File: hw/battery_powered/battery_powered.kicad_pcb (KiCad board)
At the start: 2 copper layers, 56 x 71.5 mm, 64 parts, among them J101 5077CR-16SMC2-BK-TR, J102 battery_wire_pad, J103 BM03B-SRSS-TB(LF)(SN)_pico_de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, J104 10029449-111RLF, SW101 SS12D01G4, SW102 SKRPABE010, SW103 SKRPABE010, SW104 SKRPABE010, U101 RT6150B-33GQW, U102 W25Q16JVSNIQ, U103 RP2040, U104 PCA9306D, U105 OSL10564-IB, U106 chofutech_logo, Y101 FA-238V

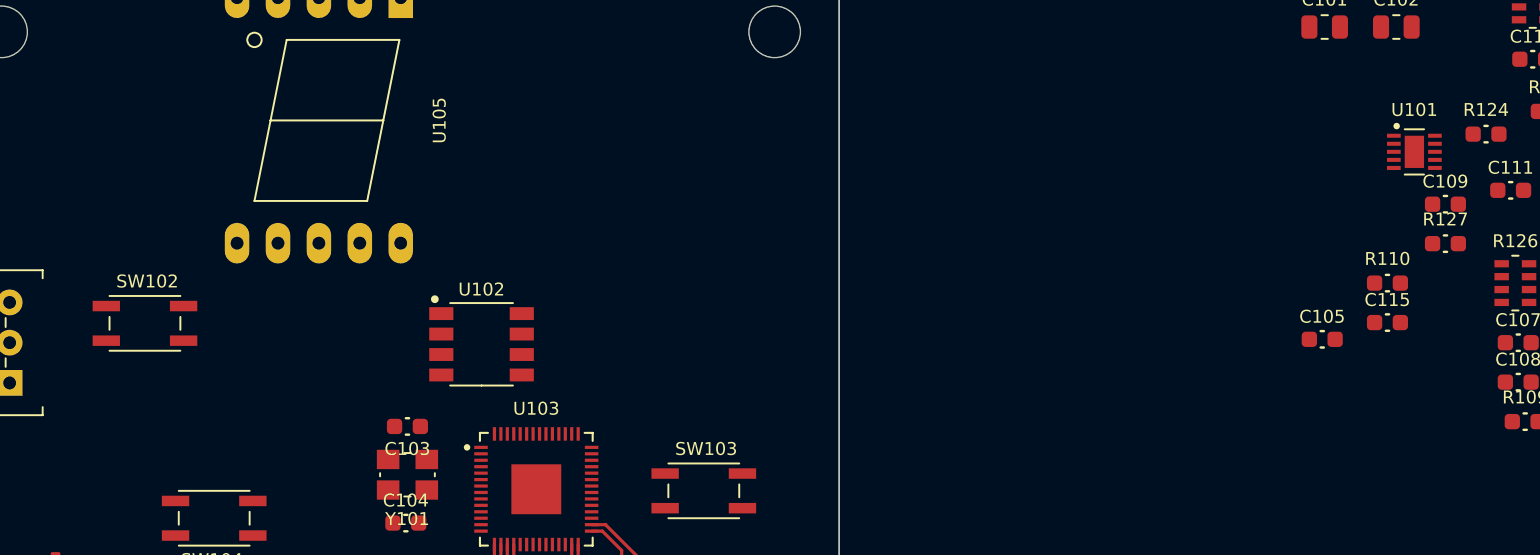
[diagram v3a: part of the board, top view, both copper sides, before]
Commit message: fixed battery_powered artwork and add .gitkeep to build dir
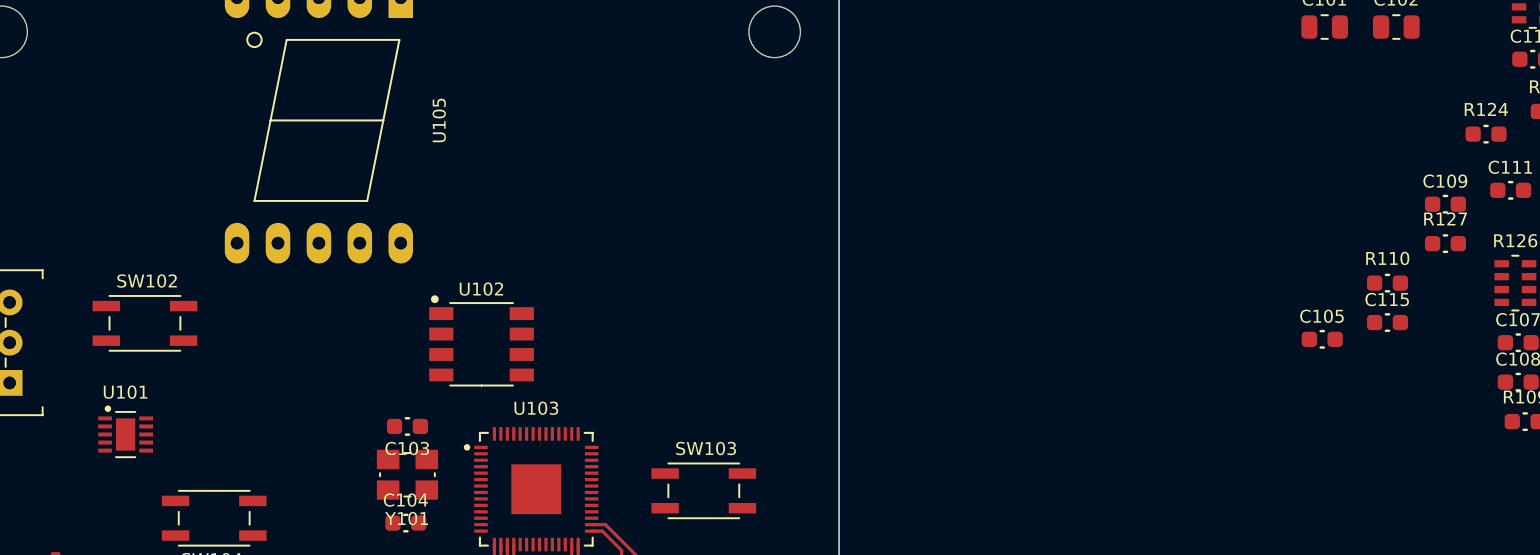
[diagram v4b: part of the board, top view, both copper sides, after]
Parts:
- moved U101 81.9 mm to (61.7, 89.0)
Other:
- copper layers 2 -> 4
- board text added: "Assumes jlcpcb 4-layer impedance control setup JLC7628. surface copper : 0.035 mm inner copper : 0.0152 mm prepreg : 0.2mm Er:4.6 core : 0.7mm Er:4.6"
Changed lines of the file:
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@@
 (kicad_pcb (version 20211014) (generator pcbnew)
   (general
-    (thickness 1.6)
+    (thickness 3.0152)
   )
   (paper "A4")
   (layers
     (0 "F.Cu" signal)
+    (1 "In1.Cu" signal)
+    (2 "In2.Cu" signal)
     (31 "B.Cu" signal)
     (32 "B.Adhes" user "B.Adhesive")
@@
       (layer "F.SilkS" (type "Top Silk Screen"))
       (layer "F.Paste" (type "Top Solder Paste"))
-      (layer "F.Mask" (type "Top Solder Mask") (thickness 0.01))
+      (layer "F.Mask" (type "Top Solder Mask") (color "Blue") (thickness 0.01))
       (layer "F.Cu" (type "copper") (thickness 0.035))
-      (layer "dielectric 1" (type "core") (thickness 1.51) (material "FR4") (epsilon_r 4.5) (loss_tangent 0.02))
+      (layer "dielectric 1" (type "prepreg") (thickness 0.2) (material "FR4") (epsilon_r 4.6) (loss_tangent 0.02))
+      (layer "In1.Cu" (type "copper") (thickness 0.0152))
+      (layer "dielectric 2" (type "core") (thickness 1) (material "FR4") (epsilon_r 4.6) (loss_tangent 0.02))
+      (layer "In2.Cu" (type "copper") (thickness 0.2))
+      (layer "dielectric 3" (type "prepreg") (thickness 1.51) (material "FR4") (epsilon_r 4.6) (loss_tangent 0.02))
       (layer "B.Cu" (type "copper") (thickness 0.035))
-      (layer "B.Mask" (type "Bottom Solder Mask") (thickness 0.01))
+      (layer "B.Mask" (type "Bottom Solder Mask") (color "Blue") (thickness 0.01))
       (layer "B.Paste" (type "Bottom Solder Paste"))
       (layer "B.SilkS" (type "Bottom Silk Screen"))
@@
   )
   (footprint "00_custom_lib:RT6150B-33GQW" (layer "F.Cu")
-    (at 141.72 71.45)
+    (at 61.7 89)
     (descr "back-boost converter, low quiescent current, 10-DFN")
     (tags "back boost converter 10-DFN")
@@
     (effects (font (size 1 1) (thickness 0.15)) (justify left mirror))
   )
+  (gr_text "Assumes jlcpcb 4-layer impedance control setup JLC7628.\nsurface copper : 0.035 mm\ninner copper : 0.0152 mm\nprepreg : 0.2mm Er:4.6\ncore : 0.7mm Er:4.6" (at 77.1 39.3) (layer "Cmts.User")
+    (effects (font (size 1 1) (thickness 0.15)))
+  )
   (segment (start 92.75 110.05) (end 93.5 109.3) (width 0.3) (layer "F.Cu") (net 19))
